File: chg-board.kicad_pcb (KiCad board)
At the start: 2 copper layers, 50 x 38 mm, 6 parts, among them J1 Conn_01x09_Male, J2 Conn_01x09_Male, J3 Conn_01x09_Male, J4 Conn_01x09_Male, J5 Conn_01x02_Female, J6 Conn_01x07_Female

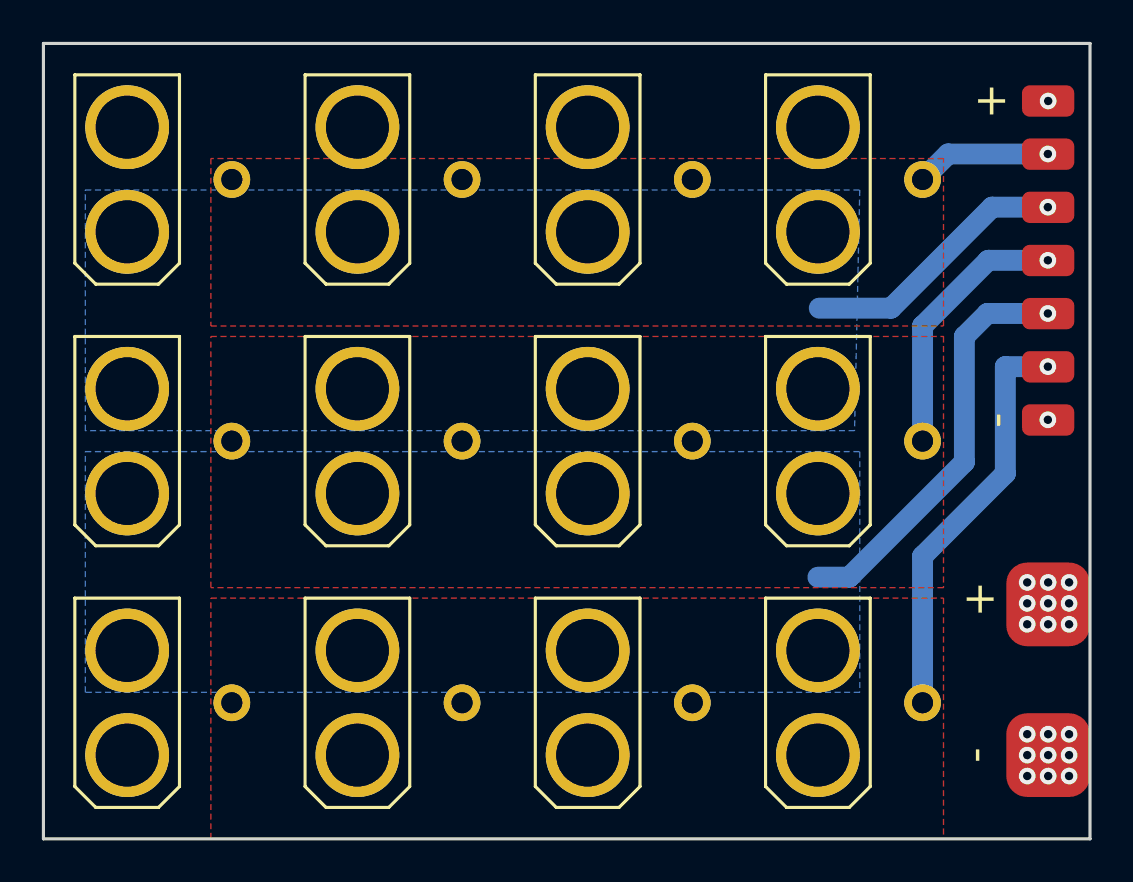
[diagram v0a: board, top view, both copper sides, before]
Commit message: Flipped GND and VCC markings to better fit ISDT SC-608
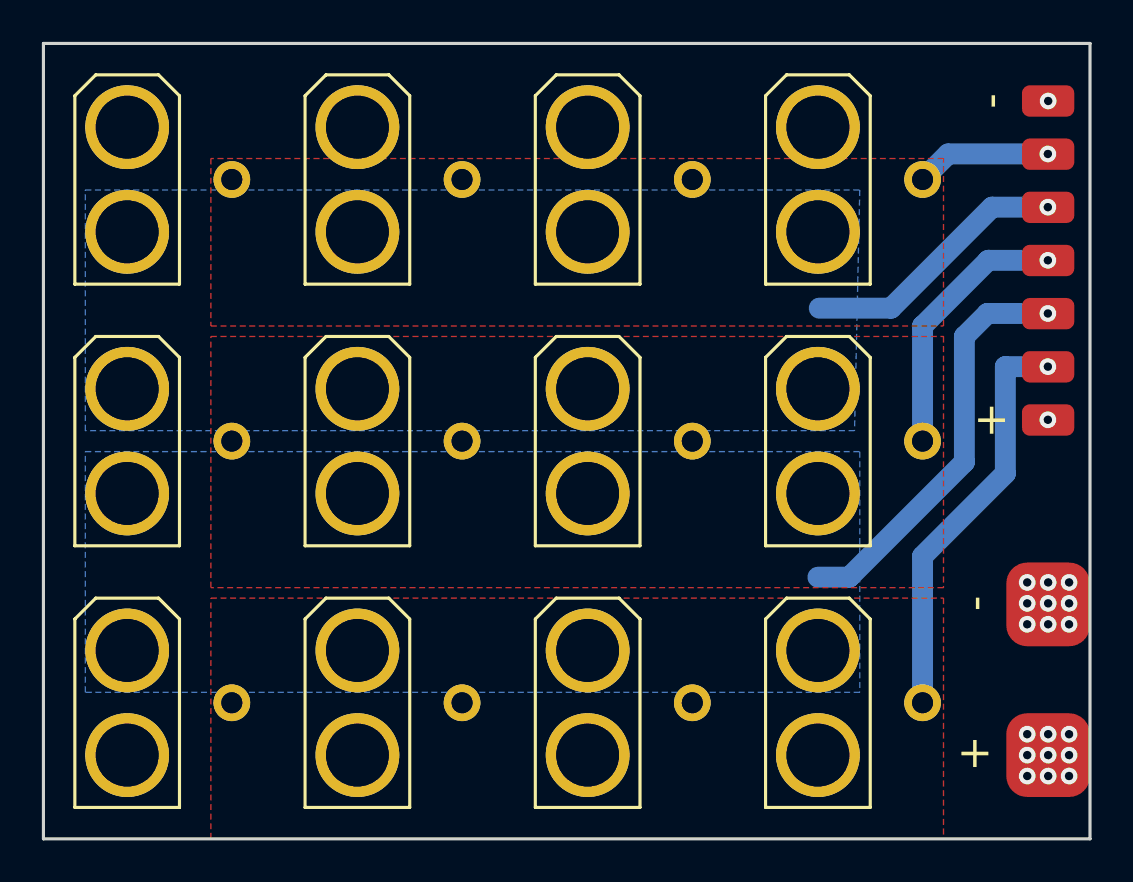
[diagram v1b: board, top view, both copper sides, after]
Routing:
- net Net-(J1-Pad8): track 19.7 -> 6.49 mm
- net Net-(J1-Pad2): track 6.49 -> 19.7 mm
- net Net-(J1-Pad6): track 19.7 -> 12.9 mm
- net Net-(J1-Pad3): track 12.9 -> 19.7 mm
- net VCC: vias 16 -> 14
- net GND: vias 14 -> 16
- added copper zone on F.Cu, net GND
- added copper zone on B.Cu, net VCC
- removed copper zone on B.Cu, net GND
- removed copper zone on F.Cu, net VCC
